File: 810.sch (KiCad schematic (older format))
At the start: 325 parts, among them J1 PJ301BM, J10 PJ301BM, J11 PJ301BM, J12 PJ301BM, J13 PJ301BM, J14 PJ301BM, J15 JACK_MONO_SW, J16 PJ301BM, J17 PJ301B, J18 PJ301B, J2 PJ301BM, J3 PJ301BM, J4 PJ301B, J5 PJ301B, J6 PJ301BM, J7 PJ301BM, J8 PJ301BM, J9 PJ301BM, P1 CONN_01X08, P2 CONN_02X05, P3 CONN_01X03, P4 CONN_01X08, P5 CONN_01X02, P6 CONN_02X03, Q1 PMBT2369, Q10 2SK208-GR, Q11 2SC4738, Q12 2SA1832, Q13 2SA1832, Q14 2SA1832, Q15 2SC4738, Q2 2SK208-GR, Q3 2SA1618, Q4 2SC4207, Q5 2SK208-GR, Q6 MMBF4391LT1G, Q7 2SA1832, Q8 PMBT2369, Q9 2SK208-GR, SW1 SPDT, SW2 SPDT, SW3 BF3-1050, SW4 SPDT, SW5 DP6T-ALPHA-SR2511, U1 TL072-, U10 TL072-, U11 TL072-, U12 TA75S558F, U13 TA75S558F, U14 TA75S558F, U15 TA75S558F, U16 TA75S558F, U17 CD4052, U18 TA75S558F, U19 TL072-, U2 TL072-, U20 CD4013, U3 TL072-, U4 CD40106, U5 CD4027, U6 LM13700, U7 LM13700, U8 LM13700, U9 TL072-

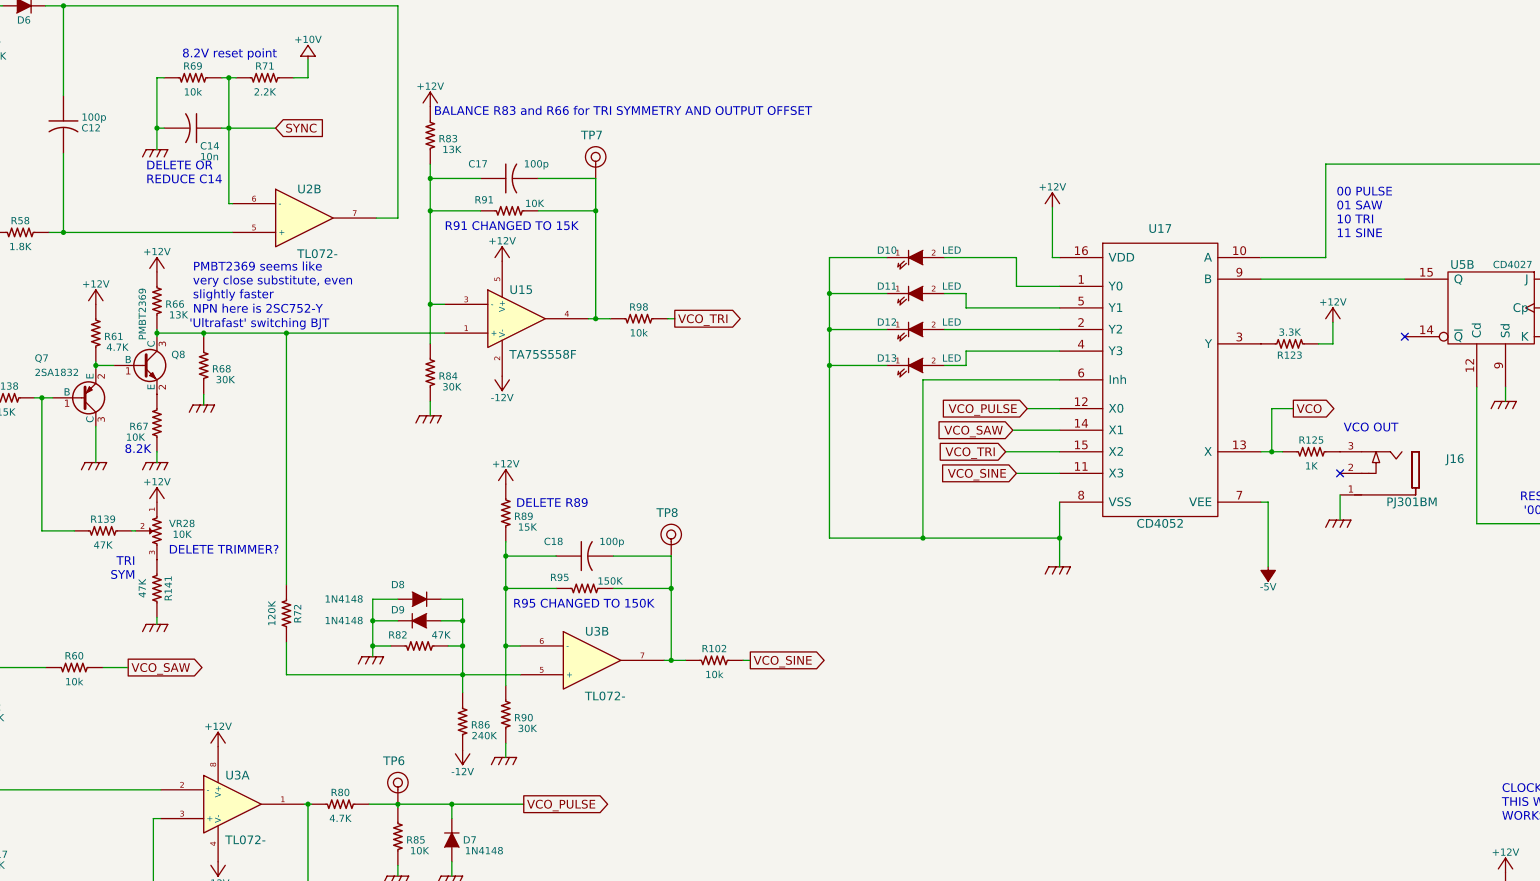
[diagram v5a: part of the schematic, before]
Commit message: changed TRI and SINE waveshapers - tested and working
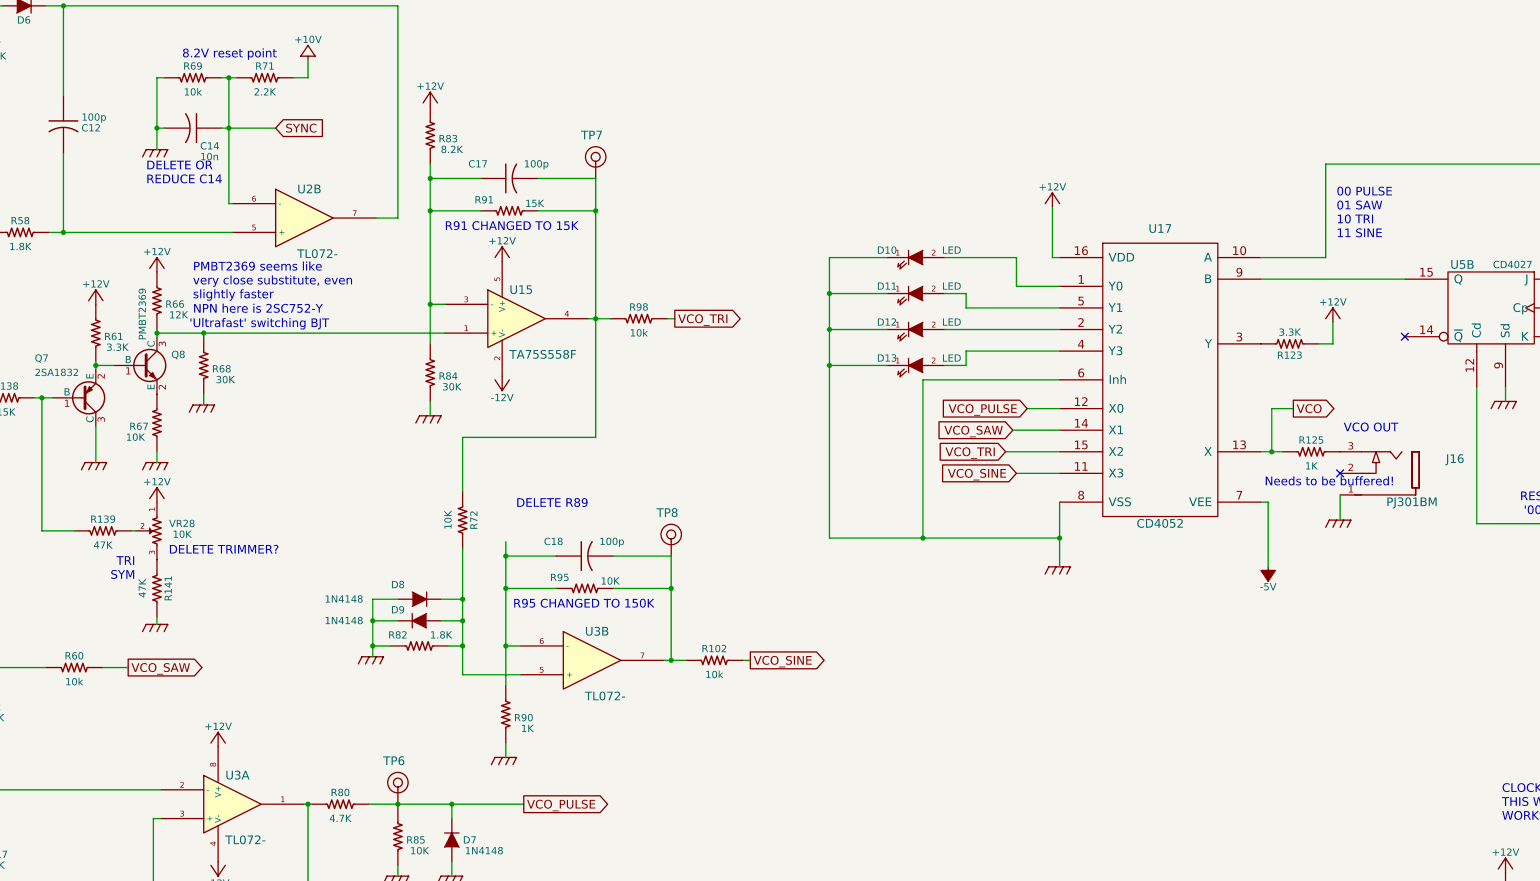
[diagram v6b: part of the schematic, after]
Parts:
- removed R86: 240K, MyModules:SM0603-R-JRL, symbol R_US
- removed R89: 15K, MyModules:SM0603-R-JRL, symbol R_US
- R61: value 4.7K -> 3.3K
- R66: value 13K -> 12K
- R72: value 120K -> 10K
- R82: value 47K -> 1.8K
- R83: value 13K -> 8.2K
- R90: value 30K -> 1K
- R91: value 10K -> 15K
- R95: value 150K -> 10K
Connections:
- net at Q8.3 (C), R66.1, R68.2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: no longer R72.1
- net at C17.2, R91.2, R98.1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: now also R72.1
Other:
- note added: "Needs to be buffered!"
- note removed: "8.2K"
- note removed: "BALANCE R83 and R66 for TRI SYMMETRY AND OUTPUT OFFSET"
- moved on the sheet: R72
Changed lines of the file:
@@
 P 14000 4025
 F 0 "R61" H 13875 4050 50  0000 C CNN
-F 1 "4.7K" H 13850 4125 50  0000 C CNN
+F 1 "3.3K" H 13850 4125 50  0000 C CNN
 F 2 "MyModules:SM0603-R-JRL" H 14000 4025 60  0001 C CNN
 F 3 "" H 14000 4025 60  0001 C CNN
@@
 P 14425 3800
 F 0 "R66" H 14300 3825 50  0000 C CNN
-F 1 "13K" H 14275 3900 50  0000 C CNN
+F 1 "12K" H 14275 3900 50  0000 C CNN
 F 2 "MyModules:SM0603-R-JRL" H 14425 3800 60  0001 C CNN
 F 3 "" H 14425 3800 60  0001 C CNN
@@
 P 16875 3175
 F 0 "R91" V 16950 3350 50  0000 C CNN
-F 1 "10K" V 16925 3000 50  0000 C CNN
+F 1 "15K" V 16925 3000 50  0000 C CNN
 F 2 "MyModules:SM0603-R-JRL" H 16875 3175 60  0001 C CNN
 F 3 "" H 16875 3175 60  0001 C CNN
@@
 P 16325 2650
 F 0 "R83" H 16200 2675 50  0000 C CNN
-F 1 "13K" H 16175 2750 50  0000 C CNN
+F 1 "8.2K" H 16175 2750 50  0000 C CNN
 F 2 "MyModules:SM0603-R-JRL" H 16325 2650 60  0001 C CNN
 F 3 "" H 16325 2650 60  0001 C CNN
@@
 P 16850 6675
 F 0 "R90" H 16725 6700 50  0000 C CNN
-F 1 "30K" H 16700 6775 50  0000 C CNN
+F 1 "1K" H 16700 6775 50  0000 C CNN
 F 2 "MyModules:SM0603-R-JRL" H 16850 6675 60  0001 C CNN
 F 3 "" H 16850 6675 60  0001 C CNN
@@
 P 17400 5800
 F 0 "R95" V 17475 5975 50  0000 C CNN
-F 1 "150K" V 17450 5625 50  0000 C CNN
+F 1 "10K" V 17450 5625 50  0000 C CNN
 F 2 "MyModules:SM0603-R-JRL" H 17400 5800 60  0001 C CNN
 F 3 "" H 17400 5800 60  0001 C CNN
@@
 $EndComp
 $Comp
-L R_US R89
-U 1 1 596972D4
-P 16850 5275
-F 0 "R89" H 16725 5300 50  0000 C CNN
-F 1 "15K" H 16700 5375 50  0000 C CNN
-F 2 "MyModules:SM0603-R-JRL" H 16850 5275 60  0001 C CNN
-F 3 "" H 16850 5275 60  0001 C CNN
-F 4 "P10.0KCCT-ND" V 16850 5275 60  0001 C CNN "Digikey"
-	1    16850 5275
-	-1   0    0    1
-$EndComp
-$Comp
-L +12V #PWR040
-U 1 1 596972DB
-P 16850 5075
-F 0 "#PWR040" H 16850 4925 50  0001 C CNN
-F 1 "+12V" H 16850 5215 50  0000 C CNN
-F 2 "" H 16850 5075 60  0000 C CNN
-F 3 "" H 16850 5075 60  0000 C CNN
-	1    16850 5075
-	1    0    0    -1
-$EndComp
-$Comp
 L TL072- U3
 U 2 1 596972E1
@@
 L R_US R72
 U 1 1 596972F3
-P 15325 5975
-F 0 "R72" V 15405 5975 50  0000 C CNN
-F 1 "120K" V 15225 5975 50  0000 C CNN
-F 2 "MyModules:SM0603-R-JRL" H 15325 5975 60  0001 C CNN
-F 3 "" H 15325 5975 60  0001 C CNN
-F 4 "P10.0KCCT-ND" V 15325 5975 60  0001 C CNN "Digikey"
-	1    15325 5975
+P 16550 5325
+F 0 "R72" V 16630 5325 50  0000 C CNN
+F 1 "10K" V 16450 5325 50  0000 C CNN
+F 2 "MyModules:SM0603-R-JRL" H 16550 5325 60  0001 C CNN
+F 3 "" H 16550 5325 60  0001 C CNN
+F 4 "P10.0KCCT-ND" V 16550 5325 60  0001 C CNN "Digikey"
+	1    16550 5325
 	1    0    0    -1
 $EndComp
 $Comp
-L R_US R86
-U 1 1 596972FB
-P 16550 6725
-F 0 "R86" H 16425 6750 50  0000 C CNN
-F 1 "240K" H 16400 6825 50  0000 C CNN
-F 2 "MyModules:SM0603-R-JRL" H 16550 6725 60  0001 C CNN
-F 3 "" H 16550 6725 60  0001 C CNN
-F 4 "P10.0KCCT-ND" V 16550 6725 60  0001 C CNN "Digikey"
-	1    16550 6725
-	-1   0    0    1
-$EndComp
-$Comp
-L -12V #PWR041
-U 1 1 59697302
-P 16550 6925
-F 0 "#PWR041" H 16550 7025 30  0001 C CNN
-F 1 "-12V" H 16550 7075 50  0000 C CNN
-F 2 "~" H 16550 6925 60  0000 C CNN
-F 3 "~" H 16550 6925 60  0000 C CNN
-	1    16550 6925
-	-1   0    0    1
-$EndComp
-$Comp
 L D D8
 U 1 1 59697308
@@
 P 16250 6200
 F 0 "R82" V 16325 6350 50  0000 C CNN
-F 1 "47K" V 16325 6050 50  0000 C CNN
+F 1 "1.8K" V 16325 6050 50  0000 C CNN
 F 2 "MyModules:SM0603-R-JRL" H 16250 6200 60  0001 C CNN
 F 3 "" H 16250 6200 60  0001 C CNN
@@
 	17425 3925 17575 3925
 Wire Wire Line
-	17475 2950 17475 3925
+	17475 2950 17475 4750
 Connection ~ 16325 3825
 Wire Wire Line
@@
 Connection ~ 16550 6025
 Wire Wire Line
-	16400 6025 16550 6025
+	16550 6025 16400 6025
 Wire Wire Line
 	16400 5875 16550 5875
-Connection ~ 16550 6400
-Wire Wire Line
-	16550 5875 16550 6525
-Wire Wire Line
-	15325 6400 16950 6400
 Wire Wire Line
 	18500 6300 18550 6300
@@
 	16850 6200 16950 6200
 Wire Wire Line
-	15325 5775 15325 4025
-Connection ~ 15325 4025
-Wire Wire Line
-	15325 6400 15325 6175
-Wire Wire Line
 	6200 2150 6425 2150
 Wire Wire Line
@@
 	0    -1   -1   0
 $EndComp
-Text Notes 14200 4875 0    60   ~ 0
-8.2K
 Text Notes 16900 5950 0    60   ~ 0
 R95 CHANGED TO 150K
@@
 Text Notes 15275 5575 2    60   ~ 0
 DELETE TRIMMER?
-Text Notes 16350 2525 0    60   ~ 0
-BALANCE R83 and R66 for TRI SYMMETRY AND OUTPUT OFFSET
 Text Notes 16075 16575 0    60   ~ 0
 CHANGE R88 to 47K?
@@
 Text Notes 17425 5250 2    60   ~ 0
 DELETE R89
+Text Notes 22125 5100 0    60   ~ 0
+Needs to be buffered!
+Wire Wire Line
+	17475 4750 16550 4750
+Wire Wire Line
+	16550 4750 16550 5125
+Connection ~ 16550 5875
+Wire Wire Line
+	16550 5525 16550 6400
+Wire Wire Line
+	16550 6400 16950 6400
 $EndSCHEMATC

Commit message: beefed up rail traces, replaced pwm rail references with +10V ref
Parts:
- added C49, C50, C51: 0.1µ, MyModules:SM0603-C-JRL, symbol C_US
- added U21: TA75S558F, MyModules:SOT753_TSOP5_SC-74A, symbol TA75S558F
- R95: value 10K -> 15K
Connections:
- net +10V: now also R55.2, VR16.1, C49.1
- net +12V: now also C50.1, U21.5 (V+); no longer R55.2, VR16.1
- net -10V: now also VR16.3
- net -12V: now also C51.2, U21.2 (V-); no longer VR16.3
- net GND: now also C49.2, C50.2, C51.1
- net VCO: now also U21.1 (+); no longer R125.1
- new net: R125.1, U21.3 (-), U21.4
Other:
- note added: "330R?"
- note added: "R95 CHANGED TO 15K"
- note added: "USE +10V\nREF HERE?"
- note removed: "DELETE R89"
- note removed: "R95 CHANGED TO 150K"
- note removed: "USE +10V REF HERE?"
- moved on the sheet: J16, R125

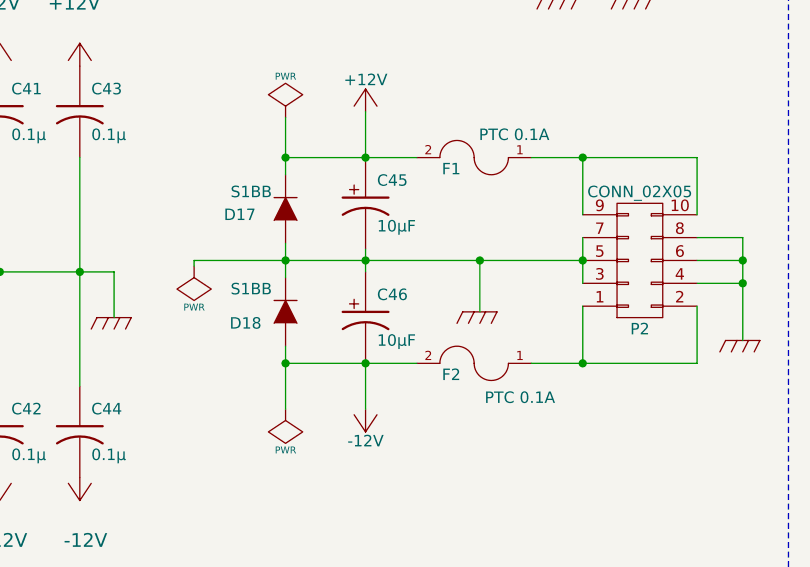
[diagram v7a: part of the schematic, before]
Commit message: moved rotary switch to its own PCB
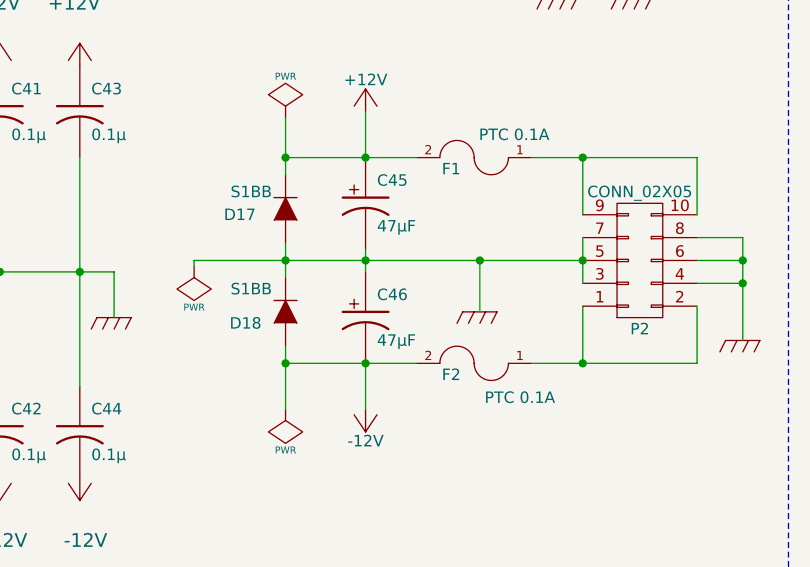
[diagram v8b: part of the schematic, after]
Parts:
- C45, C46: value 10μF -> 47μF
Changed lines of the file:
@@
 P 30775 17600
 F 0 "C45" H 30825 17700 50  0000 L CNN
-F 1 "10μF" H 30825 17500 50  0000 L CNN
+F 1 "47μF" H 30825 17500 50  0000 L CNN
 F 2 "MyModules:jrl_c_elec_5x5.3" H 30775 17600 60  0001 C CNN
 F 3 "" H 30775 17600 60  0000 C CNN
@@
 P 30775 18100
 F 0 "C46" H 30825 18200 50  0000 L CNN
-F 1 "10μF" H 30825 18000 50  0000 L CNN
+F 1 "47μF" H 30825 18000 50  0000 L CNN
 F 2 "MyModules:jrl_c_elec_5x5.3" H 30775 18100 60  0001 C CNN
 F 3 "" H 30775 18100 60  0000 C CNN
